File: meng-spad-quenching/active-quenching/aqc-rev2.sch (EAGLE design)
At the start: 287 parts, among them IC1 ADCMP582, IC10 74AHC1G04DBV, IC11 74AHC1G04DBV, IC12 TLV272DGK, IC13 TLV271DBV, IC14 74AHC1G04DBV, IC15 ALD1106, IC16 ALD1107, IC17 74AHC1G04DBV, IC18 LT1534-1, IC19 LT1534-1, IC2 TLV271DBV, IC20 STM32F411RE, IC22 TPS7A3001, IC23 74LVT126, IC24 TPS7A4901, IC25 TPS7A4901, IC26 74AHC1G14DBV, IC27 USBLC6-2SC6Y, IC28 MAX572X, IC3 NC7SV74K8X, IC4 TLV272DGK, IC5 NC7WZ16P6X, IC6 LTC1711, IC7 DS1100LU-20+, IC8 LM1117, M1 BSS806N, Q1 IRLML6402TRPBF, Q2 MMBTH81, Q3 MMBTH81, Q5 MMBTH81, Q7 MMBTH81, Q8 MMBTH81, T1 MMBTH10, T2 MMBTH10, T5 MMBTH10, T6 MMBTH10, T7 MMBTH10, T8 MMBTH10, T9 MMBTH10, U1 SN65EPT21DGK, U2 SN65EPT22DGK, U3 TPS78233DDCT, X1 CONN_SPAD, X2 CONN_PHOTON_COUNTER, X3 KEYSTONE-7774, X4 KEYSTONE-7774, X6 CONN_FORCE_QUENCH, X7 CONN_PULLDN_SENSE, X8 PN61729-S

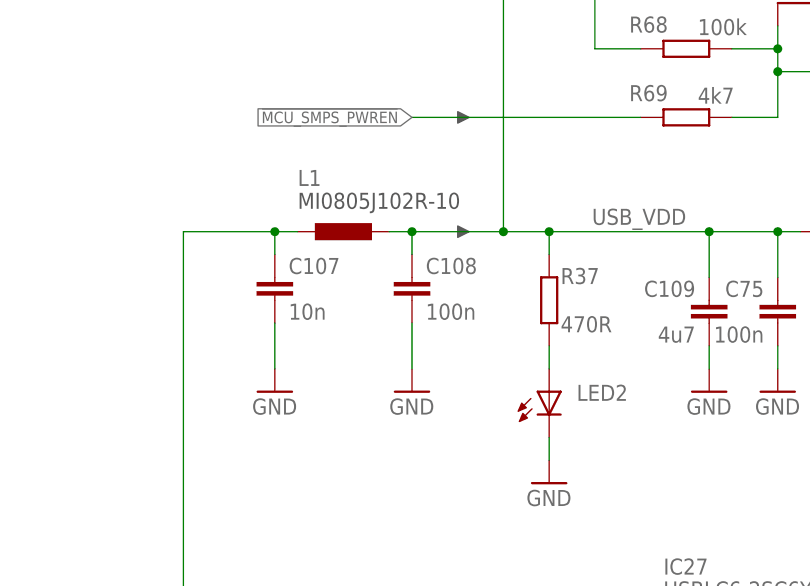
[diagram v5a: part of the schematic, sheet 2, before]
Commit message: Inrush limiter layout
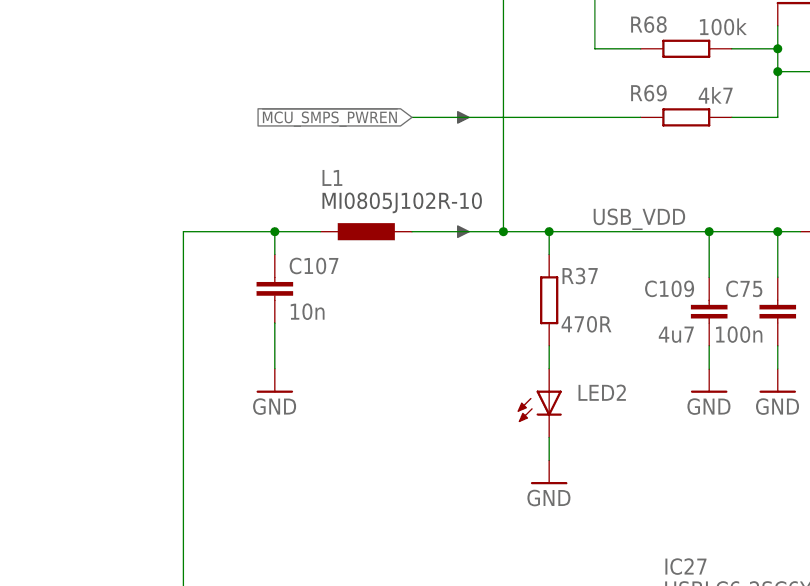
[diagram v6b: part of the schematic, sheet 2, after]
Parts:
- removed C108: 100n, rcl:C-EUC0402
- C109, C94: device rcl:C-EUC0805 -> rcl:C-EUC0603
- C93, C98: device rcl:C-EUC0402 -> rcl:C-EUC0603
- PROG: value JST_VERTICAL -> JST_VERT
- R68, R69: device resistor:R-EU_R0805 -> resistor:R-EU_R0603
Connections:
- net GND: no longer C108.2
- net USB_VDD: no longer C108.1
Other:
- moved on the sheet: L1
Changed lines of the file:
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@@
 <setting verticaltext="up"/>
 </settings>
-<grid distance="0.1" unitdist="inch" unit="inch" style="lines" multiple="1" display="yes" altdistance="0.01" altunitdist="inch" altunit="inch"/>
+<grid distance="0.1" unitdist="inch" unit="inch" style="lines" multiple="1" display="no" altdistance="0.01" altunitdist="inch" altunit="inch"/>
 <layers>
 <layer number="1" name="Top" color="4" fill="1" visible="yes" active="no"/>
@@
 <part name="DNP109" library="meng" deviceset="ARROW_1DIR" device=""/>
 <part name="DNP110" library="meng" deviceset="ARROW_1DIR" device=""/>
-<part name="PROG" library="SparkFun-Connectors" deviceset="JST_VERTICAL" device=""/>
+<part name="PROG" library="SparkFun-Connectors" deviceset="JST_VERTICAL" device="" value="JST_VERT"/>
 <part name="IC20" library="meng" deviceset="STM32F405RG" device="" value="STM32F411RE"/>
 <part name="IC27" library="meng" deviceset="USBLC6" device="" value="USBLC6-2SC6Y"/>
@@
 <part name="GND74" library="supply1" deviceset="GND" device=""/>
 <part name="GND113" library="supply1" deviceset="GND" device=""/>
-<part name="C93" library="rcl" deviceset="C-EU" device="C0402" value="100n"/>
-<part name="C98" library="rcl" deviceset="C-EU" device="C0402" value="100n"/>
+<part name="C93" library="rcl" deviceset="C-EU" device="C0603" value="100n"/>
+<part name="C98" library="rcl" deviceset="C-EU" device="C0603" value="100n"/>
 <part name="GND118" library="supply1" deviceset="GND" device=""/>
 <part name="GND119" library="supply1" deviceset="GND" device=""/>
@@
 <part name="GND75" library="supply1" deviceset="GND" device=""/>
 <part name="DNP106" library="meng" deviceset="ARROW_1DIR" device=""/>
-<part name="C94" library="rcl" deviceset="C-EU" device="C0805" value="4u7"/>
+<part name="C94" library="rcl" deviceset="C-EU" device="C0603" value="4u7"/>
 <part name="GND76" library="supply1" deviceset="GND" device=""/>
 <part name="C95" library="rcl" deviceset="C-EU" device="C0603" value="100n"/>
@@
 <part name="C107" library="rcl" deviceset="C-EU" device="C0603" value="10n"/>
 <part name="GND155" library="supply1" deviceset="GND" device=""/>
-<part name="C108" library="rcl" deviceset="C-EU" device="C0402" value="100n"/>
-<part name="GND156" library="supply1" deviceset="GND" device=""/>
 <part name="Q1" library="microbuilder" deviceset="MOSFET-P" device="WIDE" value="IRLML6402TRPBF"/>
 <part name="FRAME13" library="frames" deviceset="FRAME_A_L" device=""/>
-<part name="C109" library="rcl" deviceset="C-EU" device="C0805" value="4u7"/>
+<part name="C109" library="rcl" deviceset="C-EU" device="C0603" value="4u7"/>
 <part name="GND157" library="supply1" deviceset="GND" device=""/>
-<part name="R68" library="resistor" deviceset="R-EU_" device="R0805" value="100k"/>
-<part name="R69" library="resistor" deviceset="R-EU_" device="R0805" value="4k7"/>
+<part name="R68" library="resistor" deviceset="R-EU_" device="R0603" value="100k"/>
+<part name="R69" library="resistor" deviceset="R-EU_" device="R0603" value="4k7"/>
 <part name="C110" library="rcl" deviceset="C-EU" device="C0603" value="100n"/>
 <part name="DNP9" library="meng" deviceset="ARROW_1DIR" device=""/>
@@
 <instance part="X8" gate="G$1" x="68.58" y="91.44" rot="MR0"/>
 <instance part="GND107" gate="1" x="71.12" y="73.66"/>
-<instance part="L1" gate="G$1" x="93.98" y="144.78" smashed="yes">
-<attribute name="NAME" x="86.36" y="149.86" size="1.778" layer="95"/>
-<attribute name="VALUE" x="86.36" y="147.32" size="1.778" layer="97"/>
+<instance part="L1" gate="G$1" x="96.52" y="144.78" smashed="yes">
+<attribute name="NAME" x="88.9" y="149.86" size="1.778" layer="95"/>
+<attribute name="VALUE" x="88.9" y="147.32" size="1.778" layer="97"/>
 </instance>
 <instance part="L2" gate="G$1" x="83.82" y="83.82" smashed="yes">
@@
 </instance>
 <instance part="GND155" gate="1" x="83.82" y="127"/>
-<instance part="C108" gate="G$1" x="99.06" y="139.7" smashed="yes">
-<attribute name="NAME" x="100.584" y="140.081" size="1.778" layer="95"/>
-<attribute name="VALUE" x="100.584" y="135.001" size="1.778" layer="96"/>
-</instance>
-<instance part="GND156" gate="1" x="99.06" y="127"/>
 <instance part="DNP16" gate="G$1" x="182.88" y="144.78" smashed="yes"/>
 <instance part="IC8" gate="G$1" x="157.48" y="142.24"/>
@@
 </segment>
 <segment>
-<pinref part="GND156" gate="1" pin="GND"/>
-<pinref part="C108" gate="G$1" pin="2"/>
-<wire x1="99.06" y1="129.54" x2="99.06" y2="134.62" width="0.1524" layer="91"/>
-</segment>
-<segment>
 <pinref part="GND148" gate="1" pin="GND"/>
 <pinref part="IC8" gate="G$1" pin="GND"/>
@@
 <label x="74.295" y="96.52" size="0.8128" layer="95"/>
 <pinref part="C107" gate="G$1" pin="1"/>
-<wire x1="83.82" y1="144.78" x2="86.36" y2="144.78" width="0.1524" layer="91"/>
+<wire x1="83.82" y1="144.78" x2="88.9" y2="144.78" width="0.1524" layer="91"/>
 <wire x1="83.82" y1="142.24" x2="83.82" y2="144.78" width="0.1524" layer="91"/>
 <junction x="83.82" y="144.78"/>
@@
 <segment>
 <pinref part="L1" gate="G$1" pin="P$2"/>
-<wire x1="96.52" y1="144.78" x2="99.06" y2="144.78" width="0.1524" layer="91"/>
 <label x="129.54" y="147.32" size="1.778" layer="95" rot="R180"/>
-<pinref part="C108" gate="G$1" pin="1"/>
-<wire x1="99.06" y1="142.24" x2="99.06" y2="144.78" width="0.1524" layer="91"/>
-<junction x="99.06" y="144.78"/>
 <pinref part="IC8" gate="G$1" pin="IN"/>
 <wire x1="142.24" y1="144.78" x2="139.7" y2="144.78" width="0.1524" layer="91"/>

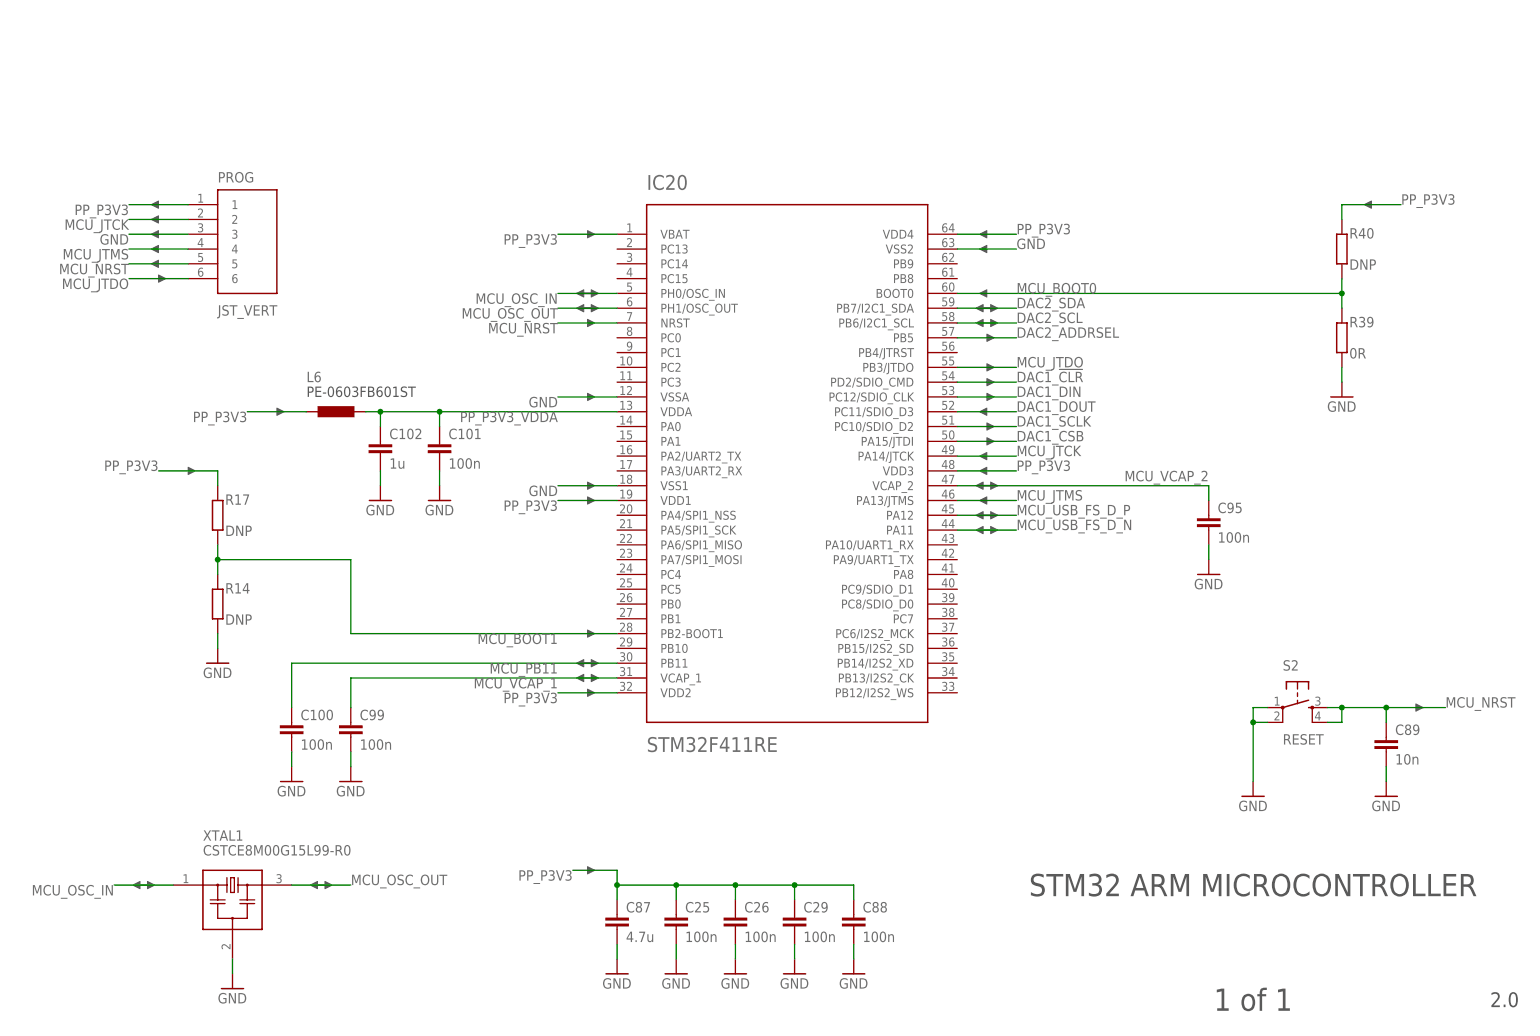
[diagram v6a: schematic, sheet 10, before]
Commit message: Routed JTAG
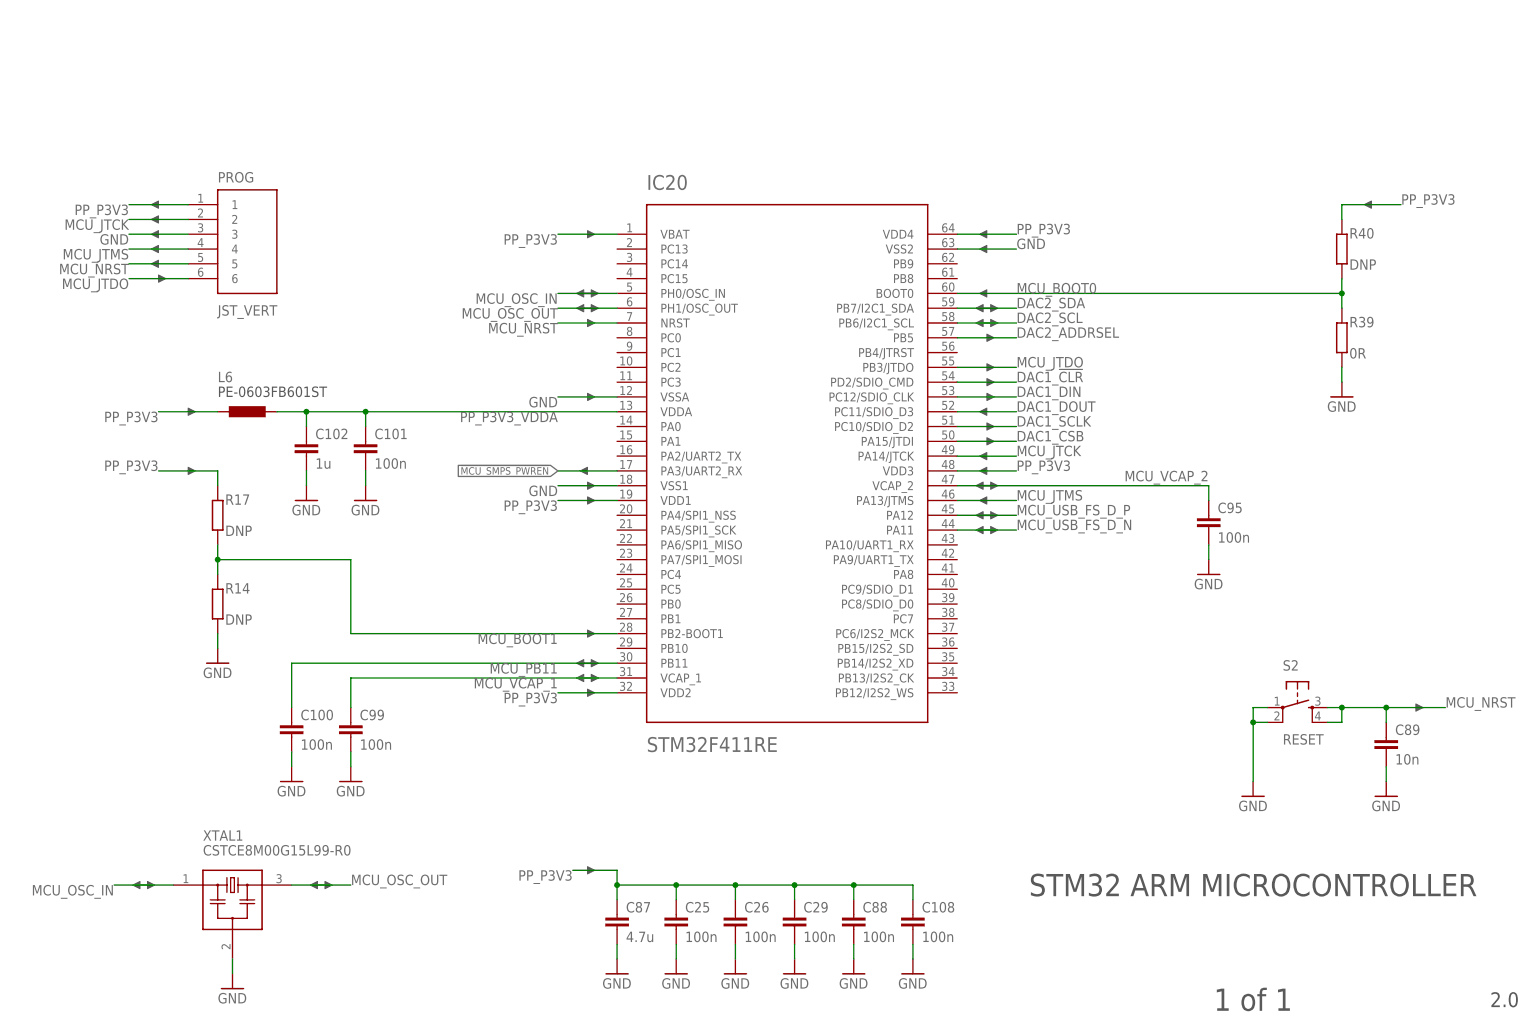
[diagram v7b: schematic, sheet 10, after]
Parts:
- added C108: 100n, rcl:C-EUC0603
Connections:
- net !MCU_SMPS_PWREN: now also IC20.PA3/UART2_RX
- net GND: now also C108.2
- net PP_P3V3: now also C108.1
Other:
- moved on the sheet: C101, C102, L6
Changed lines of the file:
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@@
 <part name="GND160" library="supply1" deviceset="GND" device=""/>
 <part name="D1" library="diode" deviceset="BAS40" device=""/>
+<part name="DNP10" library="meng" deviceset="ARROW_1DIR" device=""/>
+<part name="C108" library="rcl" deviceset="C-EU" device="C0603" value="100n"/>
+<part name="GND156" library="supply1" deviceset="GND" device=""/>
 </parts>
 <sheets>
@@
 <instance part="DNP107" gate="G$1" x="177.8" y="109.22" rot="R180"/>
 <instance part="DNP108" gate="G$1" x="177.8" y="111.76"/>
-<instance part="L6" gate="G$1" x="68.58" y="109.22" smashed="yes">
-<attribute name="NAME" x="60.96" y="114.3" size="1.778" layer="95"/>
-<attribute name="VALUE" x="60.96" y="111.76" size="1.778" layer="97"/>
+<instance part="L6" gate="G$1" x="53.34" y="109.22" smashed="yes">
+<attribute name="NAME" x="45.72" y="114.3" size="1.778" layer="95"/>
+<attribute name="VALUE" x="45.72" y="111.76" size="1.778" layer="97"/>
 </instance>
-<instance part="DNP116" gate="G$1" x="55.88" y="109.22"/>
+<instance part="DNP116" gate="G$1" x="40.64" y="109.22"/>
 <instance part="XTAL1" gate="G$1" x="48.26" y="25.4"/>
 <instance part="GND100" gate="1" x="48.26" y="10.16"/>
@@
 <instance part="U$12" gate="G$1" x="33.02" y="27.94"/>
 <instance part="U$13" gate="G$1" x="63.5" y="27.94"/>
-<instance part="C101" gate="G$1" x="83.82" y="104.14" smashed="yes">
-<attribute name="NAME" x="85.344" y="104.521" size="1.778" layer="95"/>
-<attribute name="VALUE" x="85.344" y="99.441" size="1.778" layer="96"/>
-</instance>
-<instance part="C102" gate="G$1" x="73.66" y="104.14" smashed="yes">
-<attribute name="NAME" x="75.184" y="104.521" size="1.778" layer="95"/>
-<attribute name="VALUE" x="75.184" y="99.441" size="1.778" layer="96"/>
+<instance part="C101" gate="G$1" x="71.12" y="104.14" smashed="yes">
+<attribute name="NAME" x="72.644" y="104.521" size="1.778" layer="95"/>
+<attribute name="VALUE" x="72.644" y="99.441" size="1.778" layer="96"/>
+</instance>
+<instance part="C102" gate="G$1" x="60.96" y="104.14" smashed="yes">
+<attribute name="NAME" x="62.484" y="104.521" size="1.778" layer="95"/>
+<attribute name="VALUE" x="62.484" y="99.441" size="1.778" layer="96"/>
 </instance>
-<instance part="GND109" gate="1" x="83.82" y="93.98" smashed="yes">
-<attribute name="VALUE" x="81.28" y="91.44" size="1.778" layer="96"/>
+<instance part="GND109" gate="1" x="71.12" y="93.98" smashed="yes">
+<attribute name="VALUE" x="68.58" y="91.44" size="1.778" layer="96"/>
 </instance>
-<instance part="GND110" gate="1" x="73.66" y="93.98" smashed="yes">
-<attribute name="VALUE" x="71.12" y="91.44" size="1.778" layer="96"/>
+<instance part="GND110" gate="1" x="60.96" y="93.98" smashed="yes">
+<attribute name="VALUE" x="58.42" y="91.44" size="1.778" layer="96"/>
 </instance>
 <instance part="R14" gate="G$1" x="45.72" y="76.2" smashed="yes" rot="MR270">
@@
 <instance part="DNP103" gate="G$1" x="35.56" y="134.62" rot="R180"/>
 <instance part="DNP105" gate="G$1" x="35.56" y="132.08"/>
+<instance part="DNP10" gate="G$1" x="109.22" y="99.06" rot="R180"/>
+<instance part="C108" gate="G$1" x="165.1" y="22.86" smashed="yes">
+<attribute name="NAME" x="166.624" y="23.241" size="1.778" layer="95"/>
+<attribute name="VALUE" x="166.624" y="18.161" size="1.778" layer="96"/>
+</instance>
+<instance part="GND156" gate="1" x="165.1" y="12.7" smashed="yes">
+<attribute name="VALUE" x="162.56" y="10.16" size="1.778" layer="96"/>
+</instance>
 </instances>
 <busses>
@@
 <pinref part="GND109" gate="1" pin="GND"/>
 <pinref part="C101" gate="G$1" pin="2"/>
-<wire x1="83.82" y1="96.52" x2="83.82" y2="99.06" width="0.1524" layer="91"/>
+<wire x1="71.12" y1="96.52" x2="71.12" y2="99.06" width="0.1524" layer="91"/>
 </segment>
 <segment>
 <pinref part="GND110" gate="1" pin="GND"/>
 <pinref part="C102" gate="G$1" pin="2"/>
-<wire x1="73.66" y1="96.52" x2="73.66" y2="99.06" width="0.1524" layer="91"/>
+<wire x1="60.96" y1="96.52" x2="60.96" y2="99.06" width="0.1524" layer="91"/>
 </segment>
 <segment>
@@
 <label x="30.48" y="139.7" size="1.778" layer="95" rot="R180"/>
 </segment>
+<segment>
+<pinref part="GND156" gate="1" pin="GND"/>
+<pinref part="C108" gate="G$1" pin="2"/>
+<wire x1="165.1" y1="15.24" x2="165.1" y2="17.78" width="0.1524" layer="91"/>
+</segment>
 </net>
 <net name="PP_P3V3" class="0">
@@
 <wire x1="154.94" y1="27.94" x2="154.94" y2="25.4" width="0.1524" layer="91"/>
 <junction x="144.78" y="27.94"/>
+<pinref part="C108" gate="G$1" pin="1"/>
+<wire x1="165.1" y1="25.4" x2="165.1" y2="27.94" width="0.1524" layer="91"/>
+<wire x1="165.1" y1="27.94" x2="154.94" y2="27.94" width="0.1524" layer="91"/>
+<junction x="154.94" y="27.94"/>
 </segment>
 <segment>
@@
 <segment>
 <pinref part="L6" gate="G$1" pin="P$1"/>
-<wire x1="60.96" y1="109.22" x2="50.8" y2="109.22" width="0.1524" layer="91"/>
-<label x="50.8" y="109.22" size="1.778" layer="95" rot="R180"/>
+<wire x1="45.72" y1="109.22" x2="35.56" y2="109.22" width="0.1524" layer="91"/>
+<label x="35.56" y="109.22" size="1.778" layer="95" rot="R180"/>
 </segment>
 <segment>
@@
 <pinref part="L6" gate="G$1" pin="P$2"/>
 <pinref part="IC20" gate="G$1" pin="VDDA"/>
-<wire x1="71.12" y1="109.22" x2="73.66" y2="109.22" width="0.1524" layer="91"/>
+<wire x1="55.88" y1="109.22" x2="60.96" y2="109.22" width="0.1524" layer="91"/>
 <pinref part="C102" gate="G$1" pin="1"/>
-<wire x1="73.66" y1="109.22" x2="83.82" y2="109.22" width="0.1524" layer="91"/>
-<wire x1="83.82" y1="109.22" x2="114.3" y2="109.22" width="0.1524" layer="91"/>
-<wire x1="73.66" y1="106.68" x2="73.66" y2="109.22" width="0.1524" layer="91"/>
+<wire x1="60.96" y1="109.22" x2="71.12" y2="109.22" width="0.1524" layer="91"/>
+<wire x1="71.12" y1="109.22" x2="114.3" y2="109.22" width="0.1524" layer="91"/>
+<wire x1="60.96" y1="106.68" x2="60.96" y2="109.22" width="0.1524" layer="91"/>
 <pinref part="C101" gate="G$1" pin="1"/>
-<wire x1="83.82" y1="106.68" x2="83.82" y2="109.22" width="0.1524" layer="91"/>
-<junction x="73.66" y="109.22"/>
-<junction x="83.82" y="109.22"/>
+<wire x1="71.12" y1="106.68" x2="71.12" y2="109.22" width="0.1524" layer="91"/>
+<junction x="60.96" y="109.22"/>
+<junction x="71.12" y="109.22"/>
 <label x="104.14" y="109.22" size="1.778" layer="95" rot="R180"/>
 </segment>
@@
 </segment>
 </net>
+<net name="!MCU_SMPS_PWREN" class="0">
+<segment>
+<pinref part="IC20" gate="G$1" pin="PA3/UART2_RX"/>
+<wire x1="114.3" y1="99.06" x2="104.14" y2="99.06" width="0.1524" layer="91"/>
+<label x="104.14" y="99.06" size="1.27" layer="95" rot="R180" xref="yes"/>
+</segment>
+</net>

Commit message: Misc routing
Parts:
- C17, C28: device rcl:C-EUC0402 -> rcl:C-EUC0603
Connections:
- net N$15 renamed CASC_MIDPT
- net N$24 renamed CASC_BIAS_C
- net N$30 renamed CASC_BIAS_B
- net N$35 renamed CASC_BIAS_E
- net N$75 renamed CASC_BIAS_VGND
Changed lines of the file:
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@@
 <part name="R18" library="rcl" deviceset="R-EU_" device="R0603" value="470R"/>
 <part name="DNP39" library="meng" deviceset="ARROW_1DIR" device=""/>
-<part name="C28" library="rcl" deviceset="C-EU" device="C0402" value="100n"/>
+<part name="C28" library="rcl" deviceset="C-EU" device="C0603" value="100n"/>
 <part name="GND56" library="supply1" deviceset="GND" device=""/>
 <part name="DNP40" library="meng" deviceset="ARROW_1DIR" device=""/>
@@
 <part name="R86" library="rcl" deviceset="R-EU_" device="R0603" value="100k"/>
 <part name="GND54" library="supply1" deviceset="GND" device=""/>
-<part name="C17" library="rcl" deviceset="C-EU" device="C0402" value="100n"/>
+<part name="C17" library="rcl" deviceset="C-EU" device="C0603" value="100n"/>
 <part name="GND52" library="supply1" deviceset="GND" device=""/>
 <part name="DNP112" library="meng" deviceset="ARROW_1DIR" device=""/>
@@
 </segment>
 </net>
-<net name="N$15" class="0">
+<net name="CASC_MIDPT" class="0">
 <segment>
 <pinref part="T7" gate="G$1" pin="C"/>
@@
 </segment>
 </net>
-<net name="N$24" class="0">
+<net name="CASC_BIAS_C" class="0">
 <segment>
 <pinref part="R19" gate="G$1" pin="2"/>
@@
 </segment>
 </net>
-<net name="N$30" class="0">
+<net name="CASC_BIAS_B" class="0">
 <segment>
 <pinref part="T6" gate="G$1" pin="B"/>
@@
 </segment>
 </net>
-<net name="N$35" class="0">
+<net name="CASC_BIAS_E" class="0">
 <segment>
 <pinref part="R18" gate="G$1" pin="2"/>
@@
 </segment>
 </net>
-<net name="N$75" class="0">
+<net name="CASC_BIAS_VGND" class="0">
 <segment>
 <pinref part="R85" gate="G$1" pin="2"/>
